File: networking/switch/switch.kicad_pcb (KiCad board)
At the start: 0 parts

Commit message: Feat[switch]: created all necessary symbols and footprints, started PCB
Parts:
- added C1: 10uF, Capacitor_SMD:C_0402_1005Metric, F.Cu at (126.5, 126.0)
- added C10: 0.1uF, Capacitor_SMD:C_0402_1005Metric, F.Cu at (101.3, 120.8)
- added C11: 0.1uF, Capacitor_SMD:C_0402_1005Metric, F.Cu at (101.3, 122.8)
- added C12: 22uF, Capacitor_SMD:C_0402_1005Metric, F.Cu at (104.1, 111.0)
- added C13: 0.1uF, Capacitor_SMD:C_0402_1005Metric, F.Cu at (104.1, 112.9)
- added C14: 47uF, Capacitor_SMD:C_0402_1005Metric, F.Cu at (104.1, 114.9)
- added C15: 0.1uF, Capacitor_SMD:C_0402_1005Metric, F.Cu at (104.1, 116.9)
- added C16: 0.1uF, Capacitor_SMD:C_0402_1005Metric, F.Cu at (104.1, 118.9)
- added C17: 0.1uF, Capacitor_SMD:C_0402_1005Metric, F.Cu at (104.1, 120.8)
- added C18: 0.1uF, Capacitor_SMD:C_0402_1005Metric, F.Cu at (104.1, 122.8)
- added C19: 30pF, Capacitor_SMD:C_0402_1005Metric, F.Cu at (107.0, 111.0)
- added C2: 0.1uF, Capacitor_SMD:C_0402_1005Metric, F.Cu at (126.5, 128.0)
- added C20: 30pF, Capacitor_SMD:C_0402_1005Metric, F.Cu at (107.0, 112.9)
- added C21: 0.1uF, Capacitor_SMD:C_0402_1005Metric, F.Cu at (107.0, 114.9)
- added C22: 0.1uF, Capacitor_SMD:C_0402_1005Metric, F.Cu at (107.0, 116.9)
- added C23: 0.1uF, Capacitor_SMD:C_0402_1005Metric, F.Cu at (107.0, 118.9)
- added C24: 0.1uF, Capacitor_SMD:C_0402_1005Metric, F.Cu at (129.9, 93.8)
- added C25: 0.1uF, Capacitor_SMD:C_0402_1005Metric, F.Cu at (129.9, 95.8)
- added C26: 0.1uF, Capacitor_SMD:C_0402_1005Metric, F.Cu at (129.9, 97.7)
- added C27: 0.1uF, Capacitor_SMD:C_0402_1005Metric, F.Cu at (129.9, 99.7)
- added C28: 0.1uF, Capacitor_SMD:C_0402_1005Metric, F.Cu at (129.9, 101.7)
- added C29: 1nF 2KV (1206), Capacitor_SMD:C_1206_3216Metric, F.Cu at (134.1, 94.5)
- added C3: 10uF, Capacitor_SMD:C_0402_1005Metric, F.Cu at (126.5, 130.0)
- added C30: 1nF 2KV (1206), Capacitor_SMD:C_1206_3216Metric, F.Cu at (134.1, 97.8)
- added C4: 0.1uF, Capacitor_SMD:C_0402_1005Metric, F.Cu at (126.5, 131.9)
- added C5: 0.1uF, Capacitor_SMD:C_0402_1005Metric, F.Cu at (101.3, 111.0)
- added C6: 22uF, Capacitor_SMD:C_0402_1005Metric, F.Cu at (101.3, 112.9)
- added C7: 47uF, Capacitor_SMD:C_0402_1005Metric, F.Cu at (101.3, 114.9)
- added C8: 4.7uF, Capacitor_SMD:C_0402_1005Metric, F.Cu at (101.3, 116.9)
- added C9: 10uF/NC, Capacitor_SMD:C_0402_1005Metric, F.Cu at (101.3, 118.9)
- added D1: ~, LED_SMD:LED_0603_1608Metric, F.Cu at (110.5, 121.2)
- added D2: ~, LED_SMD:LED_0603_1608Metric, F.Cu at (110.5, 123.8)
- added D3: ~, LED_SMD:LED_0603_1608Metric, F.Cu at (110.5, 126.4)
- added D4: ~, LED_SMD:LED_0603_1608Metric, F.Cu at (110.5, 129.0)
- added D5: ~, LED_SMD:LED_0603_1608Metric, F.Cu at (110.5, 131.6)
- added D6: ~, LED_SMD:LED_0603_1608Metric, F.Cu at (110.5, 134.2)
- added J1: DC IN, Connector_BarrelJack:BarrelJack_CUI_PJ-063AH_Horizontal, F.Cu at (131.6, 112.0)
- added J2: 3.3V IN, Connector_Molex:Molex_PicoBlade_53398-0271_1x02-1MP_P1.25mm_Vertical, F.Cu at (143.3, 112.9)
- added J3: PHY 5, Connector_Molex:Molex_PicoBlade_53398-0471_1x04-1MP_P1.25mm_Vertical, F.Cu at (102.0, 76.2)
- added J4: PHY 4, Connector_Molex:Molex_PicoBlade_53398-0471_1x04-1MP_P1.25mm_Vertical, F.Cu at (102.0, 83.1)
- added J5: PHY 3, Connector_Molex:Molex_PicoBlade_53398-0471_1x04-1MP_P1.25mm_Vertical, F.Cu at (102.0, 90.1)
- added J6: PHY 2, Connector_Molex:Molex_PicoBlade_53398-0471_1x04-1MP_P1.25mm_Vertical, F.Cu at (102.0, 97.0)
- added J7: PHY 1, Connector_Molex:Molex_PicoBlade_53398-0471_1x04-1MP_P1.25mm_Vertical, F.Cu at (102.0, 104.0)
- added J8: LDO IN, Connector_Molex:Molex_PicoBlade_53398-0271_1x02-1MP_P1.25mm_Vertical, F.Cu at (143.3, 119.9)
- added JP1: SEL, Jumper:SolderJumper-2_P1.3mm_Open_Pad1.0x1.5mm, F.Cu at (97.6, 111.8)
- added JP2: SEL, Jumper:SolderJumper-2_P1.3mm_Open_Pad1.0x1.5mm, F.Cu at (97.6, 115.3)
- added JP3: SEL, Jumper:SolderJumper-2_P1.3mm_Open_Pad1.0x1.5mm, F.Cu at (97.6, 118.9)
- added JP4: SEL, Jumper:SolderJumper-2_P1.3mm_Open_Pad1.0x1.5mm, F.Cu at (97.6, 122.4)
- added JP5: SEL, Jumper:SolderJumper-2_P1.3mm_Open_Pad1.0x1.5mm, F.Cu at (97.6, 126.0)
- added JP6: SEL, Jumper:SolderJumper-2_P1.3mm_Open_Pad1.0x1.5mm, F.Cu at (97.6, 129.5)
- added R1: 0, Resistor_SMD:R_0402_1005Metric, F.Cu at (109.9, 111.0)
- added R10: 75, Resistor_SMD:R_0402_1005Metric, F.Cu at (112.8, 118.9)
- added R11: 75, Resistor_SMD:R_0402_1005Metric, F.Cu at (115.7, 111.0)
- added R12: 75, Resistor_SMD:R_0402_1005Metric, F.Cu at (115.7, 113.0)
- added R13: 75, Resistor_SMD:R_0402_1005Metric, F.Cu at (115.7, 115.0)
- added R14: 75, Resistor_SMD:R_0402_1005Metric, F.Cu at (115.7, 117.0)
- added R15: 4.7k, Resistor_SMD:R_0402_1005Metric, F.Cu at (115.7, 118.9)
- added R16: 4.7k, Resistor_SMD:R_0402_1005Metric, F.Cu at (118.6, 111.0)
- added R17: 4.7k, Resistor_SMD:R_0402_1005Metric, F.Cu at (118.6, 113.0)
- added R18: 4.7k, Resistor_SMD:R_0402_1005Metric, F.Cu at (118.6, 115.0)
- added R19: 4.7k, Resistor_SMD:R_0402_1005Metric, F.Cu at (118.6, 117.0)
- added R2: 4.7k, Resistor_SMD:R_0402_1005Metric, F.Cu at (109.9, 113.0)
- added R20: 4.7k, Resistor_SMD:R_0402_1005Metric, F.Cu at (118.6, 118.9)
- added R21: 75, Resistor_SMD:R_0402_1005Metric, F.Cu at (127.0, 93.8)
- added R22: 75, Resistor_SMD:R_0402_1005Metric, F.Cu at (127.0, 95.8)
- added R23: 75, Resistor_SMD:R_0402_1005Metric, F.Cu at (127.0, 97.8)
- added R24: 75, Resistor_SMD:R_0402_1005Metric, F.Cu at (127.0, 99.8)
- added R25: 75, Resistor_SMD:R_0402_1005Metric, F.Cu at (127.0, 101.8)
- added R3: 4.7k, Resistor_SMD:R_0402_1005Metric, F.Cu at (109.9, 115.0)
- added R4: 0, Resistor_SMD:R_0402_1005Metric, F.Cu at (109.9, 117.0)
- added R5: 4.7k, Resistor_SMD:R_0402_1005Metric, F.Cu at (109.9, 118.9)
- added R6: 470K, Resistor_SMD:R_0402_1005Metric, F.Cu at (112.8, 111.0)
- added R7: 470K, Resistor_SMD:R_0402_1005Metric, F.Cu at (112.8, 113.0)
- added R8: 6.2k 1%, Resistor_SMD:R_0402_1005Metric, F.Cu at (112.8, 115.0)
- added R9: 75, Resistor_SMD:R_0402_1005Metric, F.Cu at (112.8, 117.0)
- added SW1: AFT, 6MM SW SLIM:SW_PUSH_6mm_SLIM, F.Cu at (114.5, 122.0)
- added SW2: F_PWR_OFF, 6MM SW SLIM:SW_PUSH_6mm_SLIM, F.Cu at (114.5, 126.3)
- added T1: Dual Transformer, QT24A23:QT24A23, F.Cu at (117.0, 83.0)
- added T2: Dual Transformer, QT24A23:QT24A23, F.Cu at (134.1, 83.0)
- added U1: LM1117MP-3.3, Package_TO_SOT_SMD:SOT-223-3_TabPin2, F.Cu at (143.0, 128.0)
- added U2: 24LC01, Package_TO_SOT_SMD:SOT-23-5, F.Cu at (120.3, 130.8)
- added U3: IP175G, Package_DFN_QFN:QFN-48-1EP_6x6mm_P0.4mm_EP4.3x4.3mm_ThermalVias, F.Cu at (103.9, 127.9)
- added U4: Single Transformer, BT16A07:BT16A07, F.Cu at (116.9, 100.2)
- added Y1: 25MHz, Crystal:Crystal_SMD_3225-4Pin_3.2x2.5mm, F.Cu at (115.1, 130.8)
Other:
- copper layers 0 -> 2

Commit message: Feat[switch]: initial board layout (FOLLOW @TODOs)
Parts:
- removed J2: 3.3V IN, Connector_Molex:Molex_PicoBlade_53398-0271_1x02-1MP_P1.25mm_Vertical
- added C31: 1nF 2KV (1206), Capacitor_SMD:C_1206_3216Metric, F.Cu at (160.0, 109.7)
- added C32: 1nF 2KV (1206), Capacitor_SMD:C_1206_3216Metric, F.Cu at (157.8, 86.6)
- added C33: 1nF 2KV (1206), Capacitor_SMD:C_1206_3216Metric, F.Cu at (139.2, 129.3)
- C1, C3: footprint Capacitor_SMD:C_0402_1005Metric -> Capacitor_Tantalum_SMD:CP_EIA-3216-18_Kemet-A
- C10: value 0.1uF -> 10uF/NC
- C11: value 0.1uF -> 22uF
- C12: value 22uF -> 47uF
- C14: value 47uF -> 0.1uF
- C9: value 10uF/NC -> 0.1uF
- J1: value DC IN -> LDO IN; footprint Connector_BarrelJack:BarrelJack_CUI_PJ-063AH_Horizontal -> Connector_Molex:Molex_PicoBlade_53047-0210_1x02_P1.25mm_Vertical
- J3: value PHY 5 -> 3.3V IN; footprint Connector_Molex:Molex_PicoBlade_53398-0471_1x04-1MP_P1.25mm_Vertical -> Connector_Molex:Molex_PicoBlade_53047-0210_1x02_P1.25mm_Vertical
- J4: value PHY 4 -> PHY 5; footprint Connector_Molex:Molex_PicoBlade_53398-0471_1x04-1MP_P1.25mm_Vertical -> Connector_Molex:Molex_PicoBlade_53047-0410_1x04_P1.25mm_Vertical
- J5: value PHY 3 -> PHY 4; footprint Connector_Molex:Molex_PicoBlade_53398-0471_1x04-1MP_P1.25mm_Vertical -> Connector_Molex:Molex_PicoBlade_53047-0410_1x04_P1.25mm_Vertical
- J6: value PHY 2 -> PHY 3; footprint Connector_Molex:Molex_PicoBlade_53398-0471_1x04-1MP_P1.25mm_Vertical -> Connector_Molex:Molex_PicoBlade_53047-0410_1x04_P1.25mm_Vertical
- J7: value PHY 1 -> PHY 2; footprint Connector_Molex:Molex_PicoBlade_53398-0471_1x04-1MP_P1.25mm_Vertical -> Connector_Molex:Molex_PicoBlade_53047-0410_1x04_P1.25mm_Vertical
- J8: value LDO IN -> PHY 1; footprint Connector_Molex:Molex_PicoBlade_53398-0271_1x02-1MP_P1.25mm_Vertical -> Connector_Molex:Molex_PicoBlade_53047-0410_1x04_P1.25mm_Vertical
- T1: value Dual Transformer -> QT24A23-ALT
- T2: value Dual Transformer -> QT24A23
- U4: value Single Transformer -> BT16A07
- moved J6 67.1 mm to (168.6, 105.0), turned to 90 degrees
- moved J5 66.8 mm to (168.5, 96.0), turned to 90 degrees
- moved J3 48.4 mm to (105.2, 124.5), turned to -90 degrees
- moved J7 46.5 mm to (133.7, 137.9), turned to 180 degrees
- moved T2 43.3 mm to (127.5, 125.8), turned to -90 degrees
- moved T1 41.3 mm to (155.4, 98.0)
- moved SW1 38.6 mm to (109.7, 83.7), turned to 180 degrees
- moved U1 38.4 mm to (107.7, 113.0), turned to 90 degrees
- moved D1 38.0 mm to (95.2, 86.4)
- moved D3 38.0 mm to (95.2, 91.6)
- moved D4 38.0 mm to (95.2, 94.2)
- moved D5 38.0 mm to (95.2, 96.8)
- moved D6 38.0 mm to (95.2, 99.4)
- moved D2 38.0 mm to (95.2, 89.0)
- moved C30 36.8 mm to (116.8, 130.3), turned to 90 degrees
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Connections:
- C1 pad 1: Net-(J8-Pin_2) -> Net-(J1-Pin_2)
- C10 pad 2: +3.3V -> +1.1VA
- C11 pad 1: +1.1V -> GND
- C11 pad 2: GND -> +3.3V
- C12 pad 1: GND -> +3.3V
- C12 pad 2: +3.3V -> GND
- C13 pad 1: VCC -> +1.1V
- C14 pad 1: +3.3V -> VCC
- C15 pad 1: +1.1VA -> VCC
- C16 pad 1: VCC -> GND
- C16 pad 2: GND -> /IP175G/RESETB
- C17 pad 1: GND -> VCC
- C17 pad 2: /IP175G/RESETB -> GND
- C2 pad 1: Net-(J8-Pin_2) -> Net-(J1-Pin_2)
- C23 pad 1: VCC -> +1.1VA
- C9 pad 2: +1.1VA -> +3.3V
- J1 pad 1: Net-(J8-Pin_2) -> GND
- J1 pad 2: GND -> Net-(J1-Pin_2)
- J3 pad 1: /Magnetics/TX4+ -> VCC
- J3 pad 2: /Magnetics/TX4- -> GND
- J4 pad 1: /Magnetics/TX3+ -> /Magnetics/RX4+
- J4 pad 2: /Magnetics/TX3- -> /Magnetics/RX4-
- J4 pad 3: /Magnetics/RX3+ -> /Magnetics/TX4+
- J4 pad 4: /Magnetics/RX3- -> /Magnetics/TX4-
- J5 pad 1: /Magnetics/TX2+ -> /Magnetics/RX3+
- J5 pad 2: /Magnetics/TX2- -> /Magnetics/RX3-
- J5 pad 3: /Magnetics/RX2+ -> /Magnetics/TX3+
- J5 pad 4: /Magnetics/RX2- -> /Magnetics/TX3-
- J6 pad 1: /Magnetics/TX1+ -> /Magnetics/RX2+
- J6 pad 2: /Magnetics/TX1- -> /Magnetics/RX2-
- J6 pad 3: /Magnetics/RX1+ -> /Magnetics/TX2+
- J6 pad 4: /Magnetics/RX1- -> /Magnetics/TX2-
- J7 pad 1: /Magnetics/TX0+ -> /Magnetics/RX1+
- J7 pad 2: /Magnetics/TX0- -> /Magnetics/RX1-
- J7 pad 3: /Magnetics/RX0+ -> /Magnetics/TX1+
- J7 pad 4: /Magnetics/RX0- -> /Magnetics/TX1-
- J8 pad 1: GND -> /Magnetics/RX0+
- J8 pad 2: Net-(J8-Pin_2) -> /Magnetics/RX0-
- R21 pad 1: Net-(T1-CMG0) -> Net-(R21-Pad1)
- R21 pad 2: /Magnetics/REF0 -> /Magnetics/REF3
- R22 pad 1: Net-(T1-CMG1) -> Net-(R22-Pad1)
- R22 pad 2: /Magnetics/REF0 -> /Magnetics/REF2
- R23 pad 1: Net-(T2-CMG0) -> Net-(R23-Pad1)
- R23 pad 2: /Magnetics/REF0 -> /Magnetics/REF1
- R24 pad 1: Net-(T2-CMG1) -> Net-(R24-Pad1)
- T1 pad 1: /IP175G/TXOM3 -> /Magnetics/CT3
- T1 pad 10: /IP175G/RXIP2 -> /Magnetics/CT2
- T1 pad 11: /Magnetics/RX2+ -> /IP175G/RXIM2
- T1 pad 12: /Magnetics/RX2- -> /IP175G/RXIP2
- T1 pad 13: Net-(T1-CMG1) -> /Magnetics/RX2+
- T1 pad 14: /Magnetics/TX2+ -> /Magnetics/RX2-
- T1 pad 15: /Magnetics/TX2- -> Net-(R22-Pad1)
- T1 pad 16: /Magnetics/RX3+ -> /Magnetics/TX2+
- T1 pad 17: /Magnetics/RX3- -> /Magnetics/TX2-
- T1 pad 18: Net-(T1-CMG0) -> Net-(R22-Pad1)
- T1 pad 19: /Magnetics/TX3+ -> /Magnetics/RX3+
- T1 pad 2: /IP175G/TXOP3 -> /IP175G/TXOM3
- T1 pad 20: /Magnetics/TX3- -> /Magnetics/RX3-
- T1 pad 21: (no net) -> Net-(R21-Pad1)
- T1 pad 22: (no net) -> /Magnetics/TX3+
- T1 pad 23: (no net) -> /Magnetics/TX3-
- T1 pad 24: (no net) -> Net-(R21-Pad1)
- T1 pad 3: /Magnetics/CT3 -> /IP175G/TXOP3
- T1 pad 4: /IP175G/RXIM3 -> /Magnetics/CT3
- T1 pad 5: /IP175G/RXIP3 -> /IP175G/RXIM3
- T1 pad 6: /IP175G/TXOM2 -> /IP175G/RXIP3
- T1 pad 7: /IP175G/TXOP2 -> /Magnetics/CT2
- T1 pad 8: /Magnetics/CT2 -> /IP175G/TXOM2
- T1 pad 9: /IP175G/RXIM2 -> /IP175G/TXOP2
- T2 pad 1: /IP175G/RXIP1 -> /Magnetics/CT1
- T2 pad 10: /IP175G/RXIP0 -> /Magnetics/CT0
- T2 pad 11: /Magnetics/RX0+ -> /IP175G/RXIM0
- T2 pad 12: /Magnetics/RX0- -> /IP175G/RXIP0
- T2 pad 13: Net-(T2-CMG1) -> /Magnetics/RX0+
- T2 pad 14: /Magnetics/RX0+ -> /Magnetics/RX0-
- T2 pad 15: /Magnetics/TX0- -> Net-(R24-Pad1)
- T2 pad 16: /Magnetics/TX1- -> /Magnetics/TX0+
- T2 pad 17: /Magnetics/TX1+ -> /Magnetics/TX0-
- T2 pad 18: Net-(T2-CMG0) -> Net-(R24-Pad1)
- T2 pad 19: /Magnetics/RX1- -> /Magnetics/TX1-
- T2 pad 2: /IP175G/RXIM1 -> /IP175G/RXIP1
- T2 pad 20: /Magnetics/RX1+ -> /Magnetics/TX1+
- T2 pad 21: (no net) -> Net-(R23-Pad1)
- T2 pad 22: (no net) -> /Magnetics/RX1-
- T2 pad 23: (no net) -> /Magnetics/RX1+
- T2 pad 24: (no net) -> Net-(R23-Pad1)
- T2 pad 3: /Magnetics/CT1 -> /IP175G/RXIM1
- T2 pad 4: /IP175G/TXOP1 -> /Magnetics/CT1
- T2 pad 5: /IP175G/TXOM1 -> /IP175G/TXOP1
- T2 pad 6: /IP175G/TXOM0 -> /IP175G/TXOM1
- T2 pad 7: /IP175G/TXOP0 -> /Magnetics/CT0
- T2 pad 8: /Magnetics/CT0 -> /IP175G/TXOM0
- T2 pad 9: /IP175G/RXIM0 -> /IP175G/TXOP0
- U1 pad 3: Net-(J8-Pin_2) -> Net-(J1-Pin_2)
- U4 pad 13: /Magnetics/REF4 -> unconnected-(U4-NC-Pad13)
- U4 pad 5: /Magnetics/CT4 -> unconnected-(U4-NC-Pad5)
- Y1 pad 1: Net-(U3-X2) -> Net-(U3-OSCI)
- Y1 pad 2: Net-(U3-OSCI) -> GND
- Y1 pad 3: (no net) -> Net-(U3-X2)
- Y1 pad 4: (no net) -> GND
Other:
- copper layers 2 -> 4
- board text added: "@TODO: change magnetics so that single transformer is on 0, the other two dual transformers handle 1,2,3,4"
- board text added: "@TODO: complete layout"
- board text added: "@TODO: optimize termination scheme"
- board text added: "@TODO: redesign magnetics to minimize routing and maximize signal integrity and pinout"

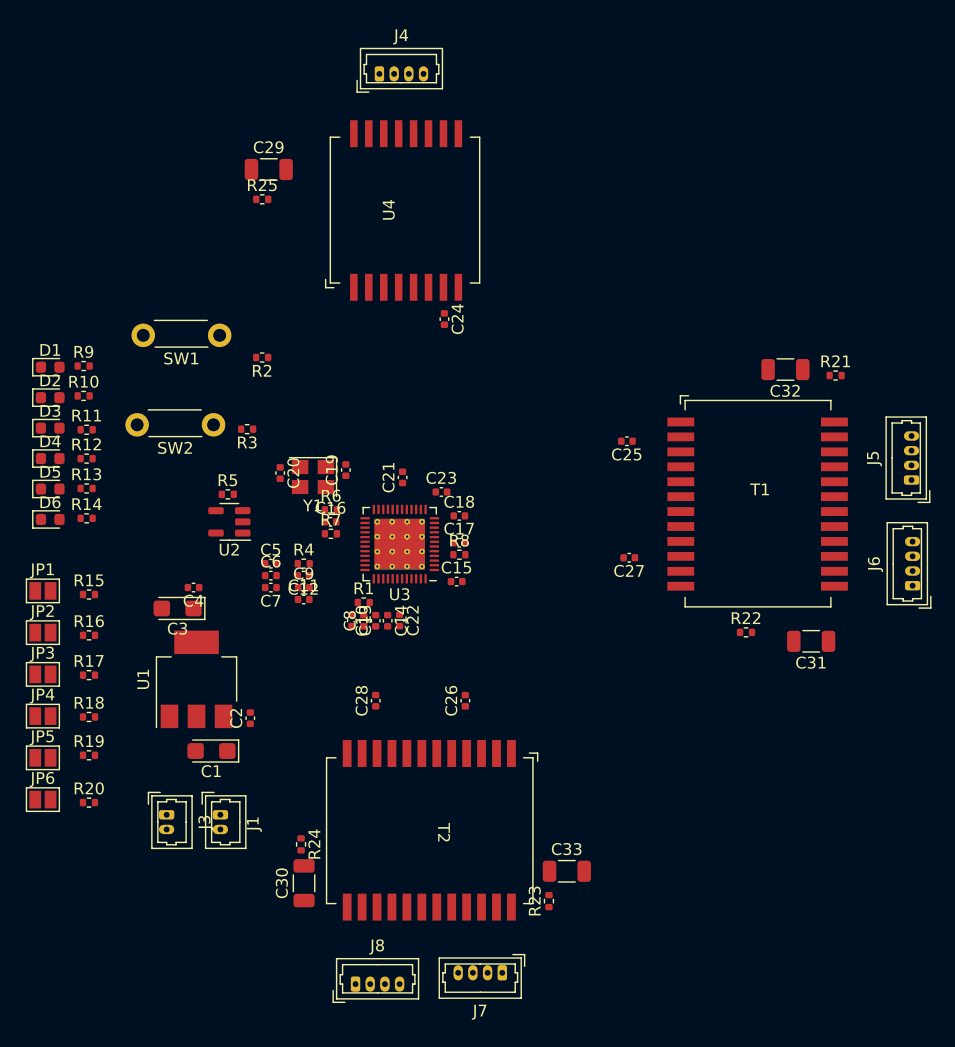
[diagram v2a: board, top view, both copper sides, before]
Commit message: Feat[switch]: initial routes
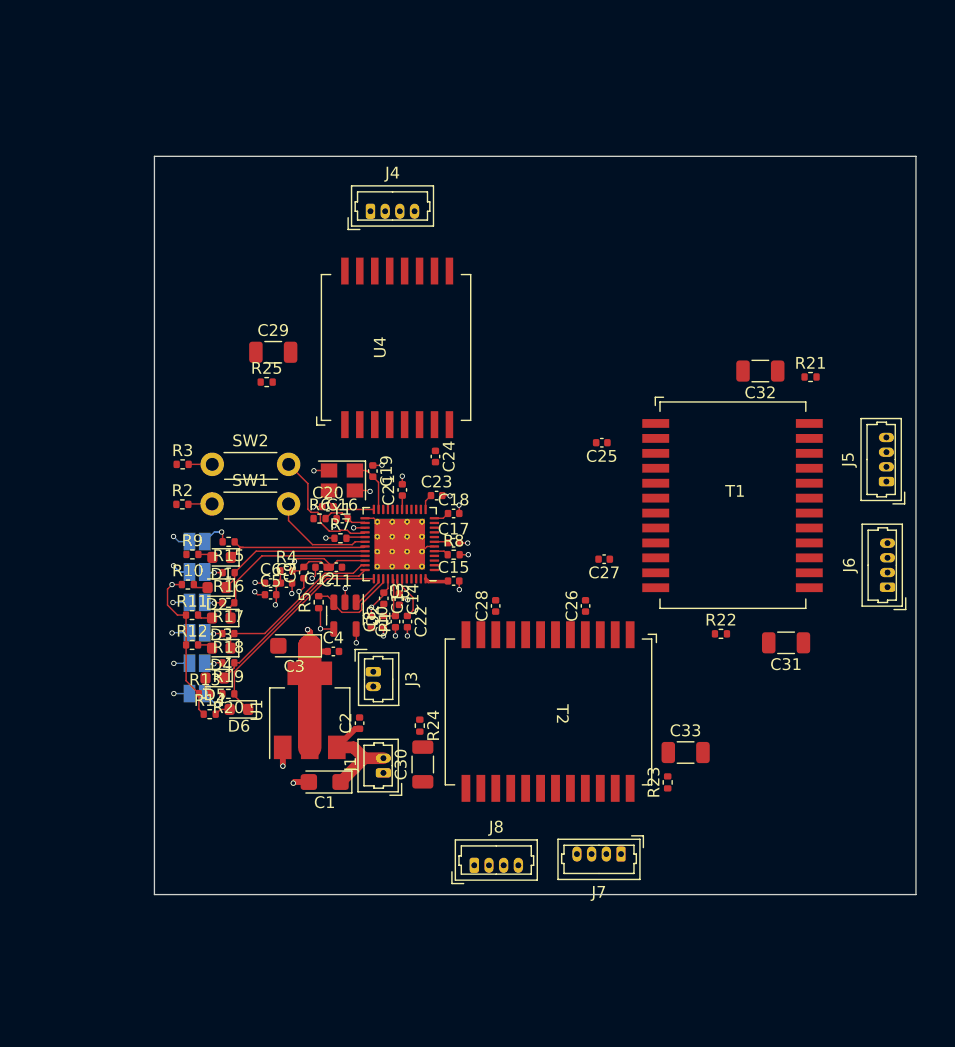
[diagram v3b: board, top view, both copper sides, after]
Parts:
- JP1, JP2, JP3, JP4, JP5, JP6: moved to B.Cu
- moved D6 22.8 mm to (111.3, 115.5), turned to 180 degrees
- moved D1 21.8 mm to (109.8, 102.6), turned to 180 degrees
- moved D3 21.7 mm to (109.8, 107.7), turned to 180 degrees
- moved D4 21.7 mm to (109.8, 110.3), turned to 180 degrees
- moved D2 21.5 mm to (109.4, 105.2), turned to 180 degrees
- moved J3 21.4 mm to (122.7, 112.3)
- moved D5 21.3 mm to (109.2, 112.9), turned to 180 degrees
- moved R13 20.1 mm to (108.4, 114.2)
- moved R14 19.7 mm to (108.8, 115.9)
- moved R9 18.5 mm to (107.3, 102.3)
- moved R10 18.3 mm to (107.0, 104.9)
- moved R12 18.2 mm to (107.3, 110.0)
- moved R11 18.1 mm to (107.3, 107.5)
- moved JP6 15.9 mm to (107.7, 114.2), turned to 180 degrees
- moved R25 15.5 mm to (113.7, 87.7)
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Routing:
- net +3.3V: track 0.00 -> 38.5 mm, vias 0 -> 3
- net VCC: track 0.00 -> 33.7 mm, vias 0 -> 3
- net GND: track 0.00 -> 33.5 mm, vias 0 -> 30
- net /IP175G/LINK_LED0: track 0.00 -> 18.8 mm
- net /IP175G/LINK_LED1/SCLK/BF_STM_DIS: track 0.00 -> 16.0 mm
- net /IP175G/LIND_LED3/Hi_PRI(1): track 0.00 -> 15.2 mm
- net /IP175G/LINK_LED2/REDUCE_IPG_EN: track 0.00 -> 15.0 mm
- net /IP175G/LINK_LED4/Hi_PRI(2): track 0.00 -> 13.4 mm
- net /IP175G/F_POWER_OFF_LED/VLAN_DIS: track 0.00 -> 13.1 mm
- net +1.1VA: track 0.00 -> 11.4 mm
- net /IP175G/F_POWER_OFF: track 0.00 -> 10.7 mm
- net Net-(J1-Pin_2): track 0.00 -> 9.80 mm
- net /IP175G/AFT: track 0.00 -> 8.87 mm
- net /IP175G/SDA: track 0.00 -> 7.82 mm
- net Net-(U3-X2): track 0.00 -> 5.06 mm
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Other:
- board outline added: 64.8 x 62.8 mm
